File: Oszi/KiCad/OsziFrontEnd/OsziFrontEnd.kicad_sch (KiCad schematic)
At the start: 12 parts

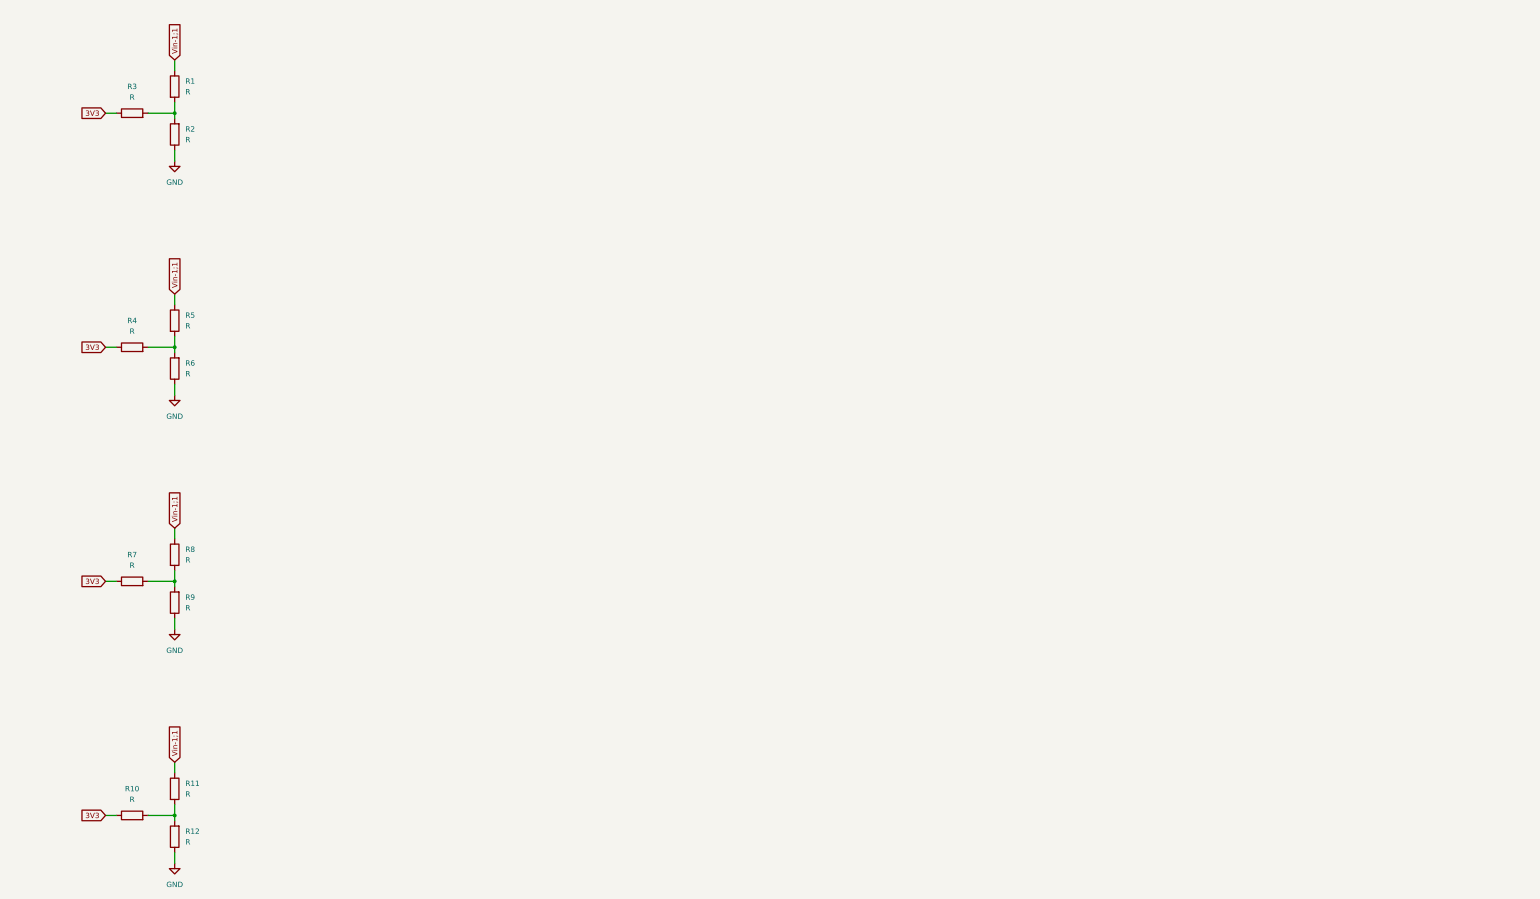
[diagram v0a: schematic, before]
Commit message: added usb-c and front end
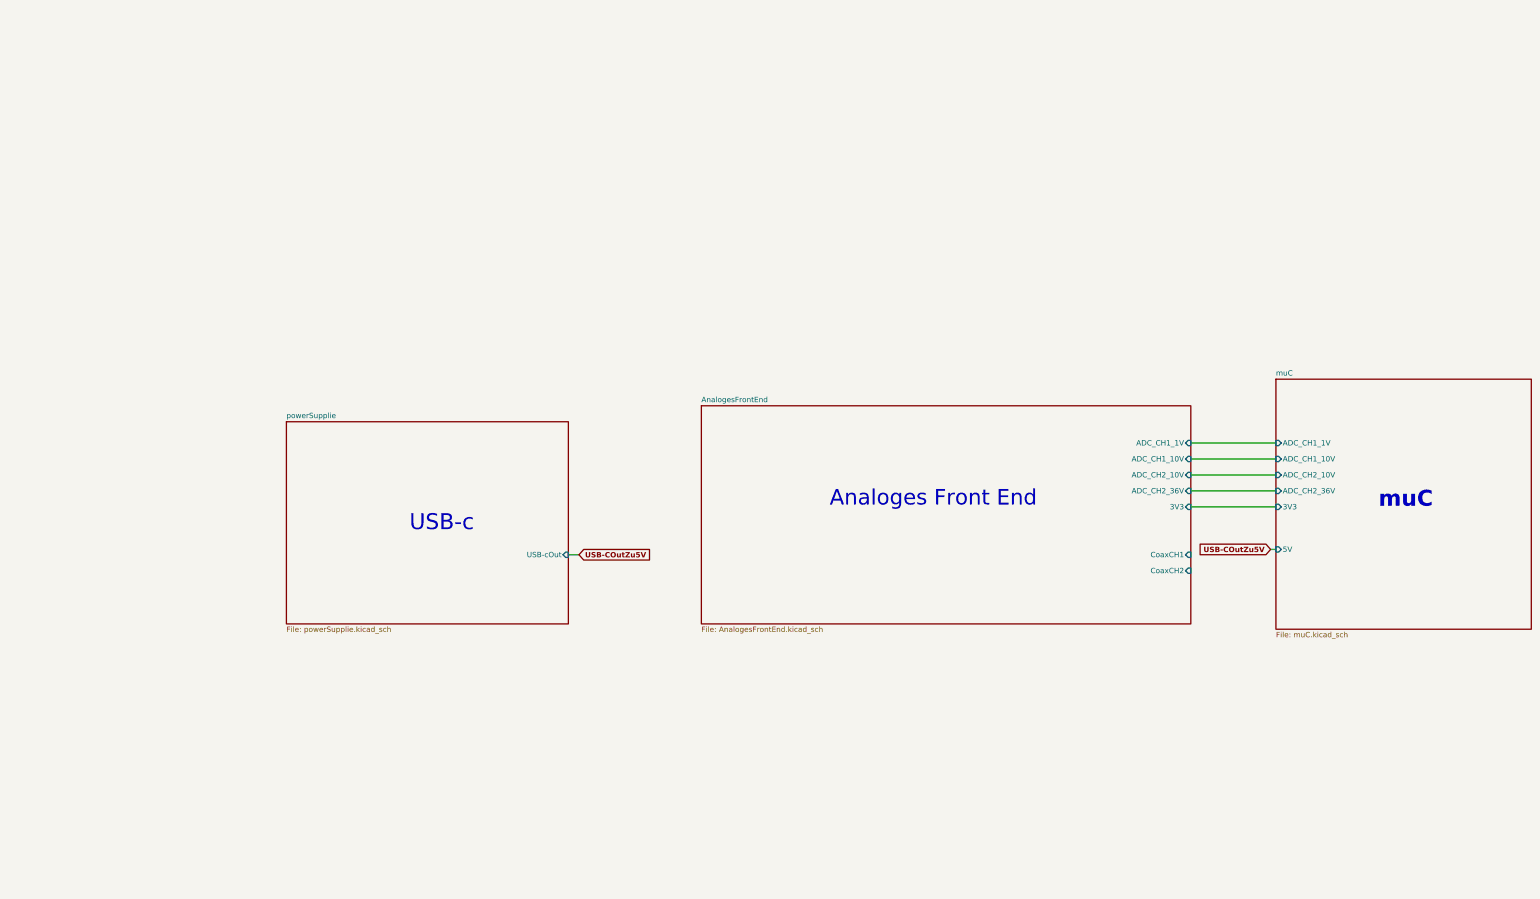
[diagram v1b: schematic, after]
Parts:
- removed R1, R10, R11, R12, R2, R3, R4, R5, R6, R7, R8, R9: R, symbol Device:R
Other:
- added sheet AnalogesFrontEnd (AnalogesFrontEnd.kicad_sch)
- added sheet muC (muC.kicad_sch)
- added sheet powerSupplie (powerSupplie.kicad_sch)
- note added: "Analoges Front End"
- note added: "USB-c"
- note added: "muC"

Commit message: startet coding and configure .ios
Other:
- added sheet Display (Display.kicad_sch)
- added sheet Ethernet (Ethernet.kicad_sch)
- sheet muC ports: added none; removed 5V
- sheet powerSupplie ports: added 3V3; removed USB-cOut
- note added: "Display"
- note added: "Eingangspannung"
- note added: "Ethernet"
- note removed: "USB-c"
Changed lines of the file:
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@@
 	(generator_version "9.0")
 	(paper "A3")
-	(text "USB-c"
-		(exclude_from_sim no)
-		(at 129.794 142.24 0)
+	(text "Eingangspannung\n"
+		(exclude_from_sim no)
+		(at 65.532 136.398 0)
 		(effects
 			(font
@@
 	(text "muC"
 		(exclude_from_sim no)
-		(at 359.918 136.652 0)
+		(at 295.656 130.81 0)
 		(effects
 			(font
@@
 	(text "Analoges Front End\n"
 		(exclude_from_sim no)
-		(at 247.142 136.398 0)
+		(at 182.88 130.556 0)
 		(effects
 			(font
@@
 		)
 	)
-	(wire
-		(pts
-			(xy 160.02 149.86) (xy 162.56 149.86)
-		)
-		(stroke
-			(width 0)
-			(type default)
-		)
-	)
-	(wire
-		(pts
-			(xy 308.61 134.62) (xy 328.93 134.62)
-		)
-		(stroke
-			(width 0)
-			(type default)
-		)
-	)
-	(wire
-		(pts
-			(xy 308.61 123.19) (xy 328.93 123.19)
-		)
-		(stroke
-			(width 0)
-			(type default)
-		)
-	)
-	(wire
-		(pts
-			(xy 327.66 148.59) (xy 328.93 148.59)
-		)
-		(stroke
-			(width 0)
-			(type default)
-		)
-	)
-	(wire
-		(pts
-			(xy 308.61 127) (xy 328.93 127)
-		)
-		(stroke
-			(width 0)
-			(type default)
-		)
-	)
-	(wire
-		(pts
-			(xy 308.61 130.81) (xy 328.93 130.81)
-		)
-		(stroke
-			(width 0)
-			(type default)
-		)
-	)
-	(wire
-		(pts
-			(xy 308.61 138.43) (xy 328.93 138.43)
-		)
-		(stroke
-			(width 0)
-			(type default)
-		)
-	)
-	(global_label "USB-COutZu5V"
+	(text "Display"
+		(exclude_from_sim no)
+		(at 293.878 203.962 0)
+		(effects
+			(font
+				(size 3.81 3.81)
+				(thickness 0.762)
+				(bold yes)
+			)
+		)
+	)
+	(text "Ethernet"
+		(exclude_from_sim no)
+		(at 302.26 53.848 0)
+		(effects
+			(font
+				(size 3.81 3.81)
+				(thickness 0.4763)
+			)
+		)
+	)
+	(junction
+		(at 254 132.588)
+		(diameter 0)
+		(color 0 0 0 0)
+	)
+	(wire
+		(pts
+			(xy 254 132.588) (xy 254 134.62)
+		)
+		(stroke
+			(width 0)
+			(type default)
+		)
+	)
+	(wire
+		(pts
+			(xy 254 132.588) (xy 264.668 132.588)
+		)
+		(stroke
+			(width 0)
+			(type default)
+		)
+	)
+	(wire
+		(pts
+			(xy 244.348 128.778) (xy 264.668 128.778)
+		)
+		(stroke
+			(width 0)
+			(type default)
+		)
+	)
+	(wire
+		(pts
+			(xy 244.348 117.348) (xy 264.668 117.348)
+		)
+		(stroke
+			(width 0)
+			(type default)
+		)
+	)
+	(wire
+		(pts
+			(xy 244.348 121.158) (xy 264.668 121.158)
+		)
+		(stroke
+			(width 0)
+			(type default)
+		)
+	)
+	(wire
+		(pts
+			(xy 244.348 124.968) (xy 264.668 124.968)
+		)
+		(stroke
+			(width 0)
+			(type default)
+		)
+	)
+	(wire
+		(pts
+			(xy 93.726 147.32) (xy 100.33 147.32)
+		)
+		(stroke
+			(width 0)
+			(type default)
+		)
+	)
+	(wire
+		(pts
+			(xy 244.348 132.588) (xy 254 132.588)
+		)
+		(stroke
+			(width 0)
+			(type default)
+		)
+	)
+	(global_label "3V3"
 		(shape input)
-		(at 327.66 148.59 180)
+		(at 254 134.62 270)
 		(fields_autoplaced yes)
 		(effects
@@
 		)
 		(property "Intersheetrefs" "${INTERSHEET_REFS}"
-			(at 309.6846 148.59 0)
+			(at 254 141.5888 90)
 			(effects
 				(font
@@
 		)
 	)
-	(global_label "USB-COutZu5V"
+	(global_label "3V3"
 		(shape input)
-		(at 162.56 149.86 0)
+		(at 100.33 147.32 0)
 		(fields_autoplaced yes)
 		(effects
@@
 		)
 		(property "Intersheetrefs" "${INTERSHEET_REFS}"
-			(at 180.5354 149.86 0)
+			(at 107.2988 147.32 0)
 			(effects
 				(font
@@
 	)
 	(sheet
-		(at 191.77 114.3)
-		(size 116.84 52.07)
+		(at 256.54 182.88)
+		(size 76.2 40.386)
 		(exclude_from_sim no)
 		(in_bom yes)
@@
 			(color 0 0 0 0.0000)
 		)
+		(property "Sheetname" "Display"
+			(at 256.54 182.1684 0)
+			(effects
+				(font
+					(size 1.27 1.27)
+				)
+				(justify left bottom)
+			)
+		)
+		(property "Sheetfile" "Display.kicad_sch"
+			(at 256.54 223.8506 0)
+			(effects
+				(font
+					(size 1.27 1.27)
+				)
+				(justify left top)
+			)
+		)
+		(instances
+			(project "OsziFrontEnd"
+				(path "/1ef80f41-06dd-4c8e-92a0-a0266e9ecde0"
+					(page "5")
+				)
+			)
+		)
+	)
+	(sheet
+		(at 127.508 108.458)
+		(size 116.84 52.07)
+		(exclude_from_sim no)
+		(in_bom yes)
+		(on_board yes)
+		(dnp no)
+		(fields_autoplaced yes)
+		(stroke
+			(width 0.1524)
+			(type solid)
+		)
+		(fill
+			(color 0 0 0 0.0000)
+		)
 		(property "Sheetname" "AnalogesFrontEnd"
-			(at 191.77 113.5884 0)
+			(at 127.508 107.7464 0)
 			(effects
 				(font
@@
 		)
 		(property "Sheetfile" "AnalogesFrontEnd.kicad_sch"
-			(at 191.77 166.9546 0)
+			(at 127.508 161.1126 0)
 			(effects
 				(font
@@
 		)
 		(pin "3V3" input
-			(at 308.61 138.43 0)
+			(at 244.348 132.588 0)
 			(effects
 				(font
@@
 		)
 		(pin "ADC_CH1_1V" input
-			(at 308.61 123.19 0)
+			(at 244.348 117.348 0)
 			(effects
 				(font
@@
 		)
 		(pin "ADC_CH1_10V" input
-			(at 308.61 127 0)
+			(at 244.348 121.158 0)
 			(effects
 				(font
@@
 		)
 		(pin "ADC_CH2_10V" input
-			(at 308.61 130.81 0)
+			(at 244.348 124.968 0)
 			(effects
 				(font
@@
 		)
 		(pin "ADC_CH2_36V" input
-			(at 308.61 134.62 0)
+			(at 244.348 128.778 0)
 			(effects
 				(font
@@
 		)
 		(pin "CoaxCH1" input
-			(at 308.61 149.86 0)
+			(at 244.348 151.638 0)
 			(effects
 				(font
@@
 		)
 		(pin "CoaxCH2" input
-			(at 308.61 153.67 0)
+			(at 244.348 155.448 0)
 			(effects
 				(font
@@
 	)
 	(sheet
-		(at 92.71 118.11)
+		(at 26.416 112.522)
 		(size 67.31 48.26)
 		(exclude_from_sim no)
@@
 		)
 		(property "Sheetname" "powerSupplie"
-			(at 92.71 117.3984 0)
+			(at 26.416 111.8104 0)
 			(effects
 				(font
@@
 		)
 		(property "Sheetfile" "powerSupplie.kicad_sch"
-			(at 92.71 166.9546 0)
+			(at 26.416 161.3666 0)
 			(effects
 				(font
@@
 			)
 		)
-		(pin "USB-cOut" input
-			(at 160.02 149.86 0)
+		(pin "3V3" output
+			(at 93.726 147.32 0)
 			(effects
 				(font
@@
 	)
 	(sheet
-		(at 328.93 107.95)
-		(size 60.96 59.69)
+		(at 262.89 33.02)
+		(size 78.232 44.45)
 		(exclude_from_sim no)
 		(in_bom yes)
@@
 			(color 0 0 0 0.0000)
 		)
+		(property "Sheetname" "Ethernet"
+			(at 262.89 32.3084 0)
+			(effects
+				(font
+					(size 1.27 1.27)
+				)
+				(justify left bottom)
+			)
+		)
+		(property "Sheetfile" "Ethernet.kicad_sch"
+			(at 262.89 78.0546 0)
+			(effects
+				(font
+					(size 1.27 1.27)
+				)
+				(justify left top)
+			)
+		)
+		(instances
+			(project "OsziFrontEnd"
+				(path "/1ef80f41-06dd-4c8e-92a0-a0266e9ecde0"
+					(page "6")
+				)
+			)
+		)
+	)
+	(sheet
+		(at 264.668 102.108)
+		(size 60.96 59.69)
+		(exclude_from_sim no)
+		(in_bom yes)
+		(on_board yes)
+		(dnp no)
+		(fields_autoplaced yes)
+		(stroke
+			(width 0.1524)
+			(type solid)
+		)
+		(fill
+			(color 0 0 0 0.0000)
+		)
 		(property "Sheetname" "muC"
-			(at 328.93 107.2384 0)
+			(at 264.668 101.3964 0)
 			(effects
 				(font
@@
 		)
 		(property "Sheetfile" "muC.kicad_sch"
-			(at 328.93 168.2246 0)
+			(at 264.668 162.3826 0)
 			(effects
 				(font
@@
 		)
 		(pin "3V3" input
-			(at 328.93 138.43 180)
+			(at 264.668 132.588 180)
 			(effects
 				(font
@@
 		)
 		(pin "ADC_CH1_1V" input
-			(at 328.93 123.19 180)
+			(at 264.668 117.348 180)
 			(effects
 				(font
@@
 		)
 		(pin "ADC_CH2_10V" input
-			(at 328.93 130.81 180)
+			(at 264.668 124.968 180)
 			(effects
 				(font
@@
 		)
 		(pin "ADC_CH2_36V" input
-			(at 328.93 134.62 180)
+			(at 264.668 128.778 180)
 			(effects
 				(font
@@
 		)
 		(pin "ADC_CH1_10V" input
-			(at 328.93 127 180)
-			(effects
-				(font
-					(size 1.27 1.27)
-				)
-				(justify left)
-			)
-		)
-		(pin "5V" input
-			(at 328.93 148.59 180)
-			(effects
-				(font
+			(at 264.668 121.158 180)
+			(effects
+				(font

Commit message: finished layout
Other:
- sheet Display ports: added 3V3, DCS, DD/C, DMISO, DMOSI, DRs, DSCK; removed none
- sheet muC ports: added DCS, DD/C, DRs, ECS, EINT, ERs, MISO, MOSI, SCK; removed none
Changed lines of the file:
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@@
+	(wire
+		(pts
+			(xy 285.75 180.34) (xy 287.02 180.34)
+		)
+		(stroke
+			(width 0)
+			(type default)
+		)
+	)
+	(wire
+		(pts
+			(xy 302.26 161.798) (xy 302.26 182.88)
+		)
+		(stroke
+			(width 0)
+			(type default)
+		)
+	)
 	(wire
 		(pts
@@
 	(wire
 		(pts
+			(xy 289.56 161.798) (xy 289.56 182.88)
+		)
+		(stroke
+			(width 0)
+			(type default)
+		)
+	)
+	(wire
+		(pts
+			(xy 287.02 182.88) (xy 287.02 180.34)
+		)
+		(stroke
+			(width 0)
+			(type default)
+		)
+	)
+	(wire
+		(pts
+			(xy 292.1 161.798) (xy 292.1 182.88)
+		)
+		(stroke
+			(width 0)
+			(type default)
+		)
+	)
+	(wire
+		(pts
+			(xy 294.64 161.798) (xy 294.64 182.88)
+		)
+		(stroke
+			(width 0)
+			(type default)
+		)
+	)
+	(wire
+		(pts
 			(xy 244.348 128.778) (xy 264.668 128.778)
 		)
@@
 	(wire
 		(pts
+			(xy 297.18 161.798) (xy 297.18 182.88)
+		)
+		(stroke
+			(width 0)
+			(type default)
+		)
+	)
+	(wire
+		(pts
 			(xy 244.348 121.158) (xy 264.668 121.158)
 		)
@@
 			(width 0)
 			(type default)
+		)
+	)
+	(wire
+		(pts
+			(xy 299.72 161.798) (xy 299.72 182.88)
+		)
+		(stroke
+			(width 0)
+			(type default)
+		)
+	)
+	(global_label "3V3"
+		(shape input)
+		(at 285.75 180.34 180)
+		(fields_autoplaced yes)
+		(effects
+			(font
+				(size 1.27 1.27)
+				(thickness 0.254)
+				(bold yes)
+			)
+			(justify right)
+		)
+		(property "Intersheetrefs" "${INTERSHEET_REFS}"
+			(at 278.7812 180.34 0)
+			(effects
+				(font
+					(size 1.27 1.27)
+				)
+				(justify right)
+				(hide yes)
+			)
 		)
 	)
@@
 			)
 		)
+		(pin "3V3" input
+			(at 287.02 182.88 90)
+			(effects
+				(font
+					(size 1.27 1.27)
+				)
+				(justify right)
+			)
+		)
+		(pin "DCS" input
+			(at 289.56 182.88 90)
+			(effects
+				(font
+					(size 1.27 1.27)
+				)
+				(justify right)
+			)
+		)
+		(pin "DD{slash}C" input
+			(at 292.1 182.88 90)
+			(effects
+				(font
+					(size 1.27 1.27)
+				)
+				(justify right)
+			)
+		)
+		(pin "DMISO" input
+			(at 294.64 182.88 90)
+			(effects
+				(font
+					(size 1.27 1.27)
+				)
+				(justify right)
+			)
+		)
+		(pin "DMOSI" input
+			(at 297.18 182.88 90)
+			(effects
+				(font
+					(size 1.27 1.27)
+				)
+				(justify right)
+			)
+		)
+		(pin "DRs" input
+			(at 299.72 182.88 90)
+			(effects
+				(font
+					(size 1.27 1.27)
+				)
+				(justify right)
+			)
+		)
+		(pin "DSCK" input
+			(at 302.26 182.88 90)
+			(effects
+				(font
+					(size 1.27 1.27)
+				)
+				(justify right)
+			)
+		)
 		(instances
 			(project "OsziFrontEnd"
@@
 			(effects
 				(font
+					(size 1.27 1.27)
+				)
+				(justify left)
+			)
+		)
+		(pin "DCS" input
+			(at 289.56 161.798 270)
+			(effects
+				(font
+					(size 1.27 1.27)
+				)
+				(justify left)
+			)
+		)
+		(pin "DD{slash}C" input
+			(at 292.1 161.798 270)
+			(effects
+				(font
+					(size 1.27 1.27)
+				)
+				(justify left)
+			)
+		)
+		(pin "DRs" input
+			(at 299.72 161.798 270)
+			(effects
+				(font
+					(size 1.27 1.27)
+				)
+				(justify left)
+			)
+		)
+		(pin "ECS" input
+			(at 296.545 102.108 90)
+			(effects
+				(font
+					(size 1.27 1.27)
+				)
+				(justify right)
+			)
+		)
+		(pin "EINT" input
+			(at 299.72 102.108 90)
+			(effects
+				(font
+					(size 1.27 1.27)
+				)
+				(justify right)
+			)
+		)
+		(pin "ERs" input
+			(at 302.895 102.108 90)
+			(effects
+				(font
+					(size 1.27 1.27)
+				)
+				(justify right)
+			)
+		)
+		(pin "MISO" input
+			(at 294.64 161.798 270)
+			(effects
+				(font
+					(size 1.27 1.27)
+				)
+				(justify left)
+			)
+		)
+		(pin "MOSI" input
+			(at 297.18 161.798 270)
+			(effects
+				(font
+					(size 1.27 1.27)
+				)
+				(justify left)
+			)
+		)
+		(pin "SCK" input
+			(at 302.26 161.798 270)
+			(effects
+				(font

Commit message: jetzt git
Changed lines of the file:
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@@
+	(wire
+		(pts
+			(xy 262.128 124.46) (xy 262.128 124.968)
+		)
+		(stroke
+			(width 0)
+			(type default)
+		)
+	)
+	(wire
+		(pts
+			(xy 260.858 121.158) (xy 244.348 121.158)
+		)
+		(stroke
+			(width 0)
+			(type default)
+		)
+	)
 	(wire
 		(pts
@@
 	(wire
 		(pts
-			(xy 302.26 161.798) (xy 302.26 182.88)
-		)
-		(stroke
-			(width 0)
-			(type default)
-		)
-	)
-	(wire
-		(pts
-			(xy 254 132.588) (xy 264.668 132.588)
-		)
-		(stroke
-			(width 0)
-			(type default)
-		)
-	)
-	(wire
-		(pts
-			(xy 289.56 161.798) (xy 289.56 182.88)
+			(xy 302.26 161.29) (xy 302.26 182.88)
+		)
+		(stroke
+			(width 0)
+			(type default)
+		)
+	)
+	(wire
+		(pts
+			(xy 254 132.08) (xy 264.668 132.08)
+		)
+		(stroke
+			(width 0)
+			(type default)
+		)
+	)
+	(wire
+		(pts
+			(xy 259.588 117.348) (xy 244.348 117.348)
+		)
+		(stroke
+			(width 0)
+			(type default)
+		)
+	)
+	(wire
+		(pts
+			(xy 260.858 120.65) (xy 260.858 121.158)
+		)
+		(stroke
+			(width 0)
+			(type default)
+		)
+	)
+	(wire
+		(pts
+			(xy 289.56 161.29) (xy 289.56 182.88)
+		)
+		(stroke
+			(width 0)
+			(type default)
+		)
+	)
+	(wire
+		(pts
+			(xy 259.588 116.84) (xy 259.588 117.348)
 		)
 		(stroke
@@
 	(wire
 		(pts
-			(xy 292.1 161.798) (xy 292.1 182.88)
-		)
-		(stroke
-			(width 0)
-			(type default)
-		)
-	)
-	(wire
-		(pts
-			(xy 294.64 161.798) (xy 294.64 182.88)
-		)
-		(stroke
-			(width 0)
-			(type default)
-		)
-	)
-	(wire
-		(pts
-			(xy 244.348 128.778) (xy 264.668 128.778)
-		)
-		(stroke
-			(width 0)
-			(type default)
-		)
-	)
-	(wire
-		(pts
-			(xy 244.348 117.348) (xy 264.668 117.348)
-		)
-		(stroke
-			(width 0)
-			(type default)
-		)
-	)
-	(wire
-		(pts
-			(xy 297.18 161.798) (xy 297.18 182.88)
-		)
-		(stroke
-			(width 0)
-			(type default)
-		)
-	)
-	(wire
-		(pts
-			(xy 244.348 121.158) (xy 264.668 121.158)
-		)
-		(stroke
-			(width 0)
-			(type default)
-		)
-	)
-	(wire
-		(pts
-			(xy 244.348 124.968) (xy 264.668 124.968)
+			(xy 292.1 161.29) (xy 292.1 182.88)
+		)
+		(stroke
+			(width 0)
+			(type default)
+		)
+	)
+	(wire
+		(pts
+			(xy 263.398 128.27) (xy 263.398 128.778)
+		)
+		(stroke
+			(width 0)
+			(type default)
+		)
+	)
+	(wire
+		(pts
+			(xy 294.64 161.29) (xy 294.64 182.88)
+		)
+		(stroke
+			(width 0)
+			(type default)
+		)
+	)
+	(wire
+		(pts
+			(xy 263.398 128.27) (xy 264.668 128.27)
+		)
+		(stroke
+			(width 0)
+			(type default)
+		)
+	)
+	(wire
+		(pts
+			(xy 259.588 116.84) (xy 264.668 116.84)
+		)
+		(stroke
+			(width 0)
+			(type default)
+		)
+	)
+	(wire
+		(pts
+			(xy 263.398 128.778) (xy 244.348 128.778)
+		)
+		(stroke
+			(width 0)
+			(type default)
+		)
+	)
+	(wire
+		(pts
+			(xy 254 132.08) (xy 254 132.588)
+		)
+		(stroke
+			(width 0)
+			(type default)
+		)
+	)
+	(wire
+		(pts
+			(xy 297.18 161.29) (xy 297.18 182.88)
+		)
+		(stroke
+			(width 0)
+			(type default)
+		)
+	)
+	(wire
+		(pts
+			(xy 260.858 120.65) (xy 264.668 120.65)
+		)
+		(stroke
+			(width 0)
+			(type default)
+		)
+	)
+	(wire
+		(pts
+			(xy 262.128 124.46) (xy 264.668 124.46)
 		)
 		(stroke
@@
 	(wire
 		(pts
-			(xy 299.72 161.798) (xy 299.72 182.88)
+			(xy 299.72 161.29) (xy 299.72 182.88)
+		)
+		(stroke
+			(width 0)
+			(type default)
+		)
+	)
+	(wire
+		(pts
+			(xy 262.128 124.968) (xy 244.348 124.968)
 		)
 		(stroke
@@
 	)
 	(sheet
-		(at 264.668 102.108)
+		(at 264.668 101.6)
 		(size 60.96 59.69)
 		(exclude_from_sim no)
@@
 		)
 		(property "Sheetname" "muC"
-			(at 264.668 101.3964 0)
+			(at 264.668 100.8884 0)
 			(effects
 				(font
@@
 		)
 		(property "Sheetfile" "muC.kicad_sch"
-			(at 264.668 162.3826 0)
+			(at 264.668 161.8746 0)
 			(effects
 				(font
@@
 		)
 		(pin "3V3" input
-			(at 264.668 132.588 180)
+			(at 264.668 132.08 180)
 			(effects
 				(font
@@
 		)
 		(pin "ADC_CH1_1V" input
-			(at 264.668 117.348 180)
+			(at 264.668 116.84 180)
 			(effects
 				(font
@@
 		)
 		(pin "ADC_CH2_10V" input
-			(at 264.668 124.968 180)
+			(at 264.668 124.46 180)
 			(effects
 				(font
@@
 		)
 		(pin "ADC_CH2_36V" input
-			(at 264.668 128.778 180)
+			(at 264.668 128.27 180)
 			(effects
 				(font
@@
 		)
 		(pin "ADC_CH1_10V" input
-			(at 264.668 121.158 180)
+			(at 264.668 120.65 180)
 			(effects
 				(font
@@
 		)
 		(pin "DCS" input
-			(at 289.56 161.798 270)
+			(at 289.56 161.29 270)
 			(effects
 				(font
@@
 		)
 		(pin "DD{slash}C" input
-			(at 292.1 161.798 270)
+			(at 292.1 161.29 270)
 			(effects
 				(font
@@
 		)
 		(pin "DRs" input
-			(at 299.72 161.798 270)
+			(at 299.72 161.29 270)
 			(effects
 				(font
@@
 		)
 		(pin "ECS" input
-			(at 296.545 102.108 90)
+			(at 296.545 101.6 90)
 			(effects
 				(font
@@
 		)
 		(pin "EINT" input
-			(at 299.72 102.108 90)
+			(at 299.72 101.6 90)
 			(effects
 				(font
@@
 		)
 		(pin "ERs" input
-			(at 302.895 102.108 90)
+			(at 302.895 101.6 90)
 			(effects
 				(font
@@
 		)
 		(pin "MISO" input
-			(at 294.64 161.798 270)
+			(at 294.64 161.29 270)
 			(effects
 				(font
@@
 		)
 		(pin "MOSI" input
-			(at 297.18 161.798 270)
+			(at 297.18 161.29 270)
 			(effects
 				(font
@@
 		)
 		(pin "SCK" input
-			(at 302.26 161.798 270)
-			(effects
-				(font
+			(at 302.26 161.29 270)
+			(effects
+				(font
